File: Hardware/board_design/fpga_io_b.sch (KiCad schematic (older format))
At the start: 9 parts, among them P1 CONN_01X06, U1 XC7AxxT-xCSG325, U2 S25Q

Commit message: rescured and remaped symbols
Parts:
- C51: symbol C -> Device:C
- D2, D3, D4: symbol LED -> Device:LED
- P1: symbol CONN_01X06 -> PicoEVB-rescue:CONN_01X06-PicoEVB-rescue
- RN2, RN3: symbol R_Pack04 -> Device:R_Pack04
- U1: symbol xc7a50tcsg325 -> PicoEVB-rescue:xc7a50tcsg325-xc7a50t-bga325
- U2: symbol W25Q -> PicoEVB-rescue:W25Q-W25Q
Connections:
- wire segments 60 -> 74
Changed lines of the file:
@@
-EESchema Schematic File Version 2
-LIBS:power
-LIBS:device
-LIBS:transistors
-LIBS:conn
-LIBS:linear
-LIBS:regul
-LIBS:74xx
-LIBS:cmos4000
-LIBS:adc-dac
-LIBS:memory
-LIBS:xilinx
-LIBS:microcontrollers
-LIBS:dsp
-LIBS:microchip
-LIBS:analog_switches
-LIBS:motorola
-LIBS:texas
-LIBS:intel
-LIBS:audio
-LIBS:interface
-LIBS:digital-audio
-LIBS:philips
-LIBS:display
-LIBS:cypress
-LIBS:siliconi
-LIBS:opto
-LIBS:atmel
-LIBS:contrib
-LIBS:valves
-LIBS:Zilog
-LIBS:zetex
-LIBS:Xicor
-LIBS:Worldsemi
-LIBS:wiznet
-LIBS:video
-LIBS:ttl_ieee
-LIBS:transf
-LIBS:switches
-LIBS:supertex
-LIBS:stm32
-LIBS:stm8
-LIBS:silabs
-LIBS:sensors
-LIBS:rfcom
-LIBS:relays
-LIBS:references
-LIBS:pspice
-LIBS:Power_Management
-LIBS:powerint
-LIBS:Oscillators
-LIBS:onsemi
-LIBS:nxp_armmcu
-LIBS:nordicsemi
-LIBS:msp430
-LIBS:motors
-LIBS:motor_drivers
-LIBS:microchip_pic32mcu
-LIBS:microchip_pic18mcu
-LIBS:microchip_pic16mcu
-LIBS:microchip_pic12mcu
-LIBS:microchip_pic10mcu
-LIBS:microchip_dspic33dsc
-LIBS:mechanical
-LIBS:maxim
-LIBS:logo
-LIBS:Lattice
-LIBS:ir
-LIBS:hc11
-LIBS:graphic
-LIBS:gennum
-LIBS:ftdi
-LIBS:ESD_Protection
-LIBS:elec-unifil
-LIBS:diode
-LIBS:dc-dc
-LIBS:cmos_ieee
-LIBS:brooktre
-LIBS:bosch
-LIBS:bbd
-LIBS:battery_management
-LIBS:analog_devices
-LIBS:Altera
-LIBS:allegro
-LIBS:actel
-LIBS:ac-dc
-LIBS:74xgxx
-LIBS:xc7a50t-bga325
-LIBS:MAX1589A
-LIBS:MIC47050
-LIBS:TS3L110
-LIBS:W25Q
-LIBS:93LC46B-SOT23
-LIBS:m2-board
-LIBS:ft2232-fixed
-LIBS:tps82084
-LIBS:PicoEVB-cache
-EELAYER 25 0
+EESchema Schematic File Version 4
+EELAYER 30 0
 EELAYER END
-$Descr A 11000 8500
+$Descr A3 16535 11693
 encoding utf-8
 Sheet 4 7
@@
 $EndDescr
 $Comp
-L xc7a50tcsg325 U1
+L PicoEVB-rescue:xc7a50tcsg325-xc7a50t-bga325 U1
 U 4 1 586A5920
 P 5300 2900
@@
 $EndComp
 $Comp
-L xc7a50tcsg325 U1
+L PicoEVB-rescue:xc7a50tcsg325-xc7a50t-bga325 U1
 U 3 1 586A5977
 P 2550 1300
@@
 $EndComp
 $Comp
-L xc7a50tcsg325 U1
+L PicoEVB-rescue:xc7a50tcsg325-xc7a50t-bga325 U1
 U 2 1 594F31E6
 P 8600 1300
@@
 VCC_BANK14_B
 $Comp
-L GND #PWR023
+L power:GND #PWR023
 U 1 1 594F321A
 P 5650 1700
@@
 $EndComp
 $Comp
-L C C51
+L Device:C C51
 U 1 1 586D021A
 P 5950 1550
@@
 NoConn ~ 5300 7800
 $Comp
-L W25Q U2
+L PicoEVB-rescue:W25Q-W25Q U2
 U 1 1 587CA7B7
 P 6750 1400
@@
 NoConn ~ 8600 4100
 $Comp
-L LED D4
+L Device:LED D4
 U 1 1 587E337E
 P 8150 6000
@@
 $EndComp
 $Comp
-L LED D3
+L Device:LED D3
 U 1 1 594F3235
 P 8150 5700
@@
 $EndComp
 $Comp
-L LED D2
+L Device:LED D2
 U 1 1 587E3396
 P 8150 5300
@@
 NoConn ~ 8600 4800
 $Comp
-L CONN_01X06 P1
+L PicoEVB-rescue:CONN_01X06-PicoEVB-rescue P1
 U 1 1 59AB5657
 P 1350 4200
+AR Path="/59AB5657" Ref="P1"  Part="1"
+AR Path="/594F323A/59AB5657" Ref="P1"  Part="1"
 F 0 "P1" H 1350 4550 50  0000 C CNN
 F 1 "CONN_01X06" V 1450 4200 50  0000 C CNN
@@
 $EndComp
 $Comp
-L GND #PWR024
+L power:GND #PWR024
 U 1 1 59AB565E
 P 1400 4000
@@
 M2_LED_2
 Wire Wire Line
-	7250 6300 8600 6300
+	7250 6300 7400 6300
 Wire Wire Line
 	2400 6300 2550 6300
 Wire Wire Line
-	5800 1400 6450 1400
+	5800 1400 5950 1400
 Connection ~ 5950 1400
 Wire Wire Line
-	5650 1700 6450 1700
+	5650 1700 5950 1700
 Connection ~ 5950 1700
 Wire Wire Line
@@
 	6300 2300 6300 1600
 Wire Wire Line
-	6450 1500 6150 1500
+	6450 1500 6350 1500
 Wire Wire Line
 	6150 1500 6150 2400
@@
 	8600 1500 7250 1500
 Wire Wire Line
-	8600 1600 7250 1600
-Wire Wire Line
-	8600 1700 7250 1700
+	8600 1600 8000 1600
+Wire Wire Line
+	8600 1700 8100 1700
 Wire Wire Line
 	8350 1800 8600 1800
@@
 	5450 6100 5300 6100
 $Comp
-L R_Pack04 RN2
+L Device:R_Pack04 RN2
 U 1 1 59EAB957
 P 7600 5900
@@
 	7900 5300 8000 5300
 Wire Wire Line
-	7400 5700 7400 6300
+	7400 5700 7400 5800
 Connection ~ 7400 6300
 Connection ~ 7400 5800
@@
 	7800 6000 7800 6200
 $Comp
-L R_Pack04 RN3
+L Device:R_Pack04 RN3
 U 1 1 59EAF829
 P 7650 1100
@@
 	6200 850  7450 850
 Wire Wire Line
-	7450 850  7450 1200
+	7450 850  7450 900
 Connection ~ 6200 1400
 Connection ~ 7450 900
@@
 Connection ~ 8100 1700
 NoConn ~ 7850 900
+Wire Wire Line
+	5950 1400 6200 1400
+Wire Wire Line
+	5950 1700 6400 1700
+Wire Wire Line
+	6400 1700 6450 1700
+Wire Wire Line
+	7400 6300 8600 6300
+Wire Wire Line
+	7400 5800 7400 5900
+Wire Wire Line
+	7400 5900 7400 6000
+Wire Wire Line
+	7400 6000 7400 6300
+Wire Wire Line
+	6200 1400 6450 1400
+Wire Wire Line
+	7450 900  7450 1000
+Wire Wire Line
+	7450 1000 7450 1100
+Wire Wire Line
+	7450 1100 7450 1200
+Wire Wire Line
+	6350 1500 6150 1500
+Wire Wire Line
+	8000 1600 7250 1600
+Wire Wire Line
+	8100 1700 7250 1700
 $EndSCHEMATC

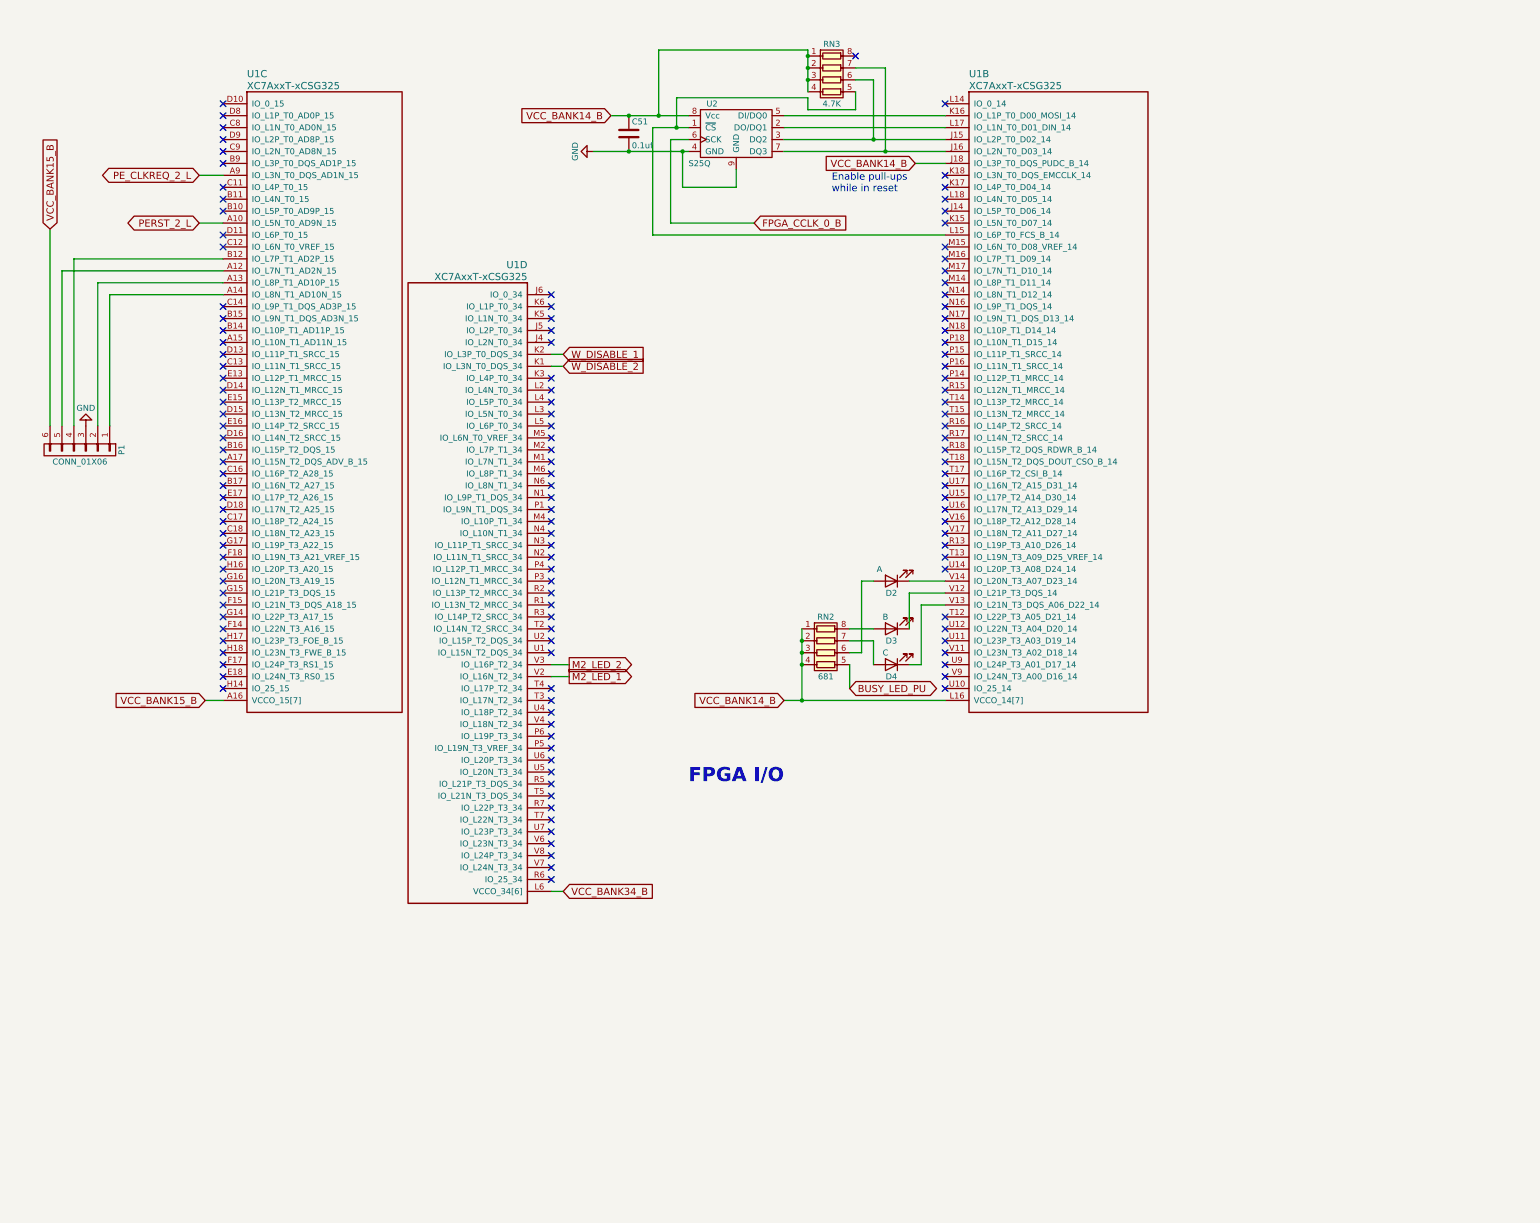
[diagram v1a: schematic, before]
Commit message: Added LPSDRAM
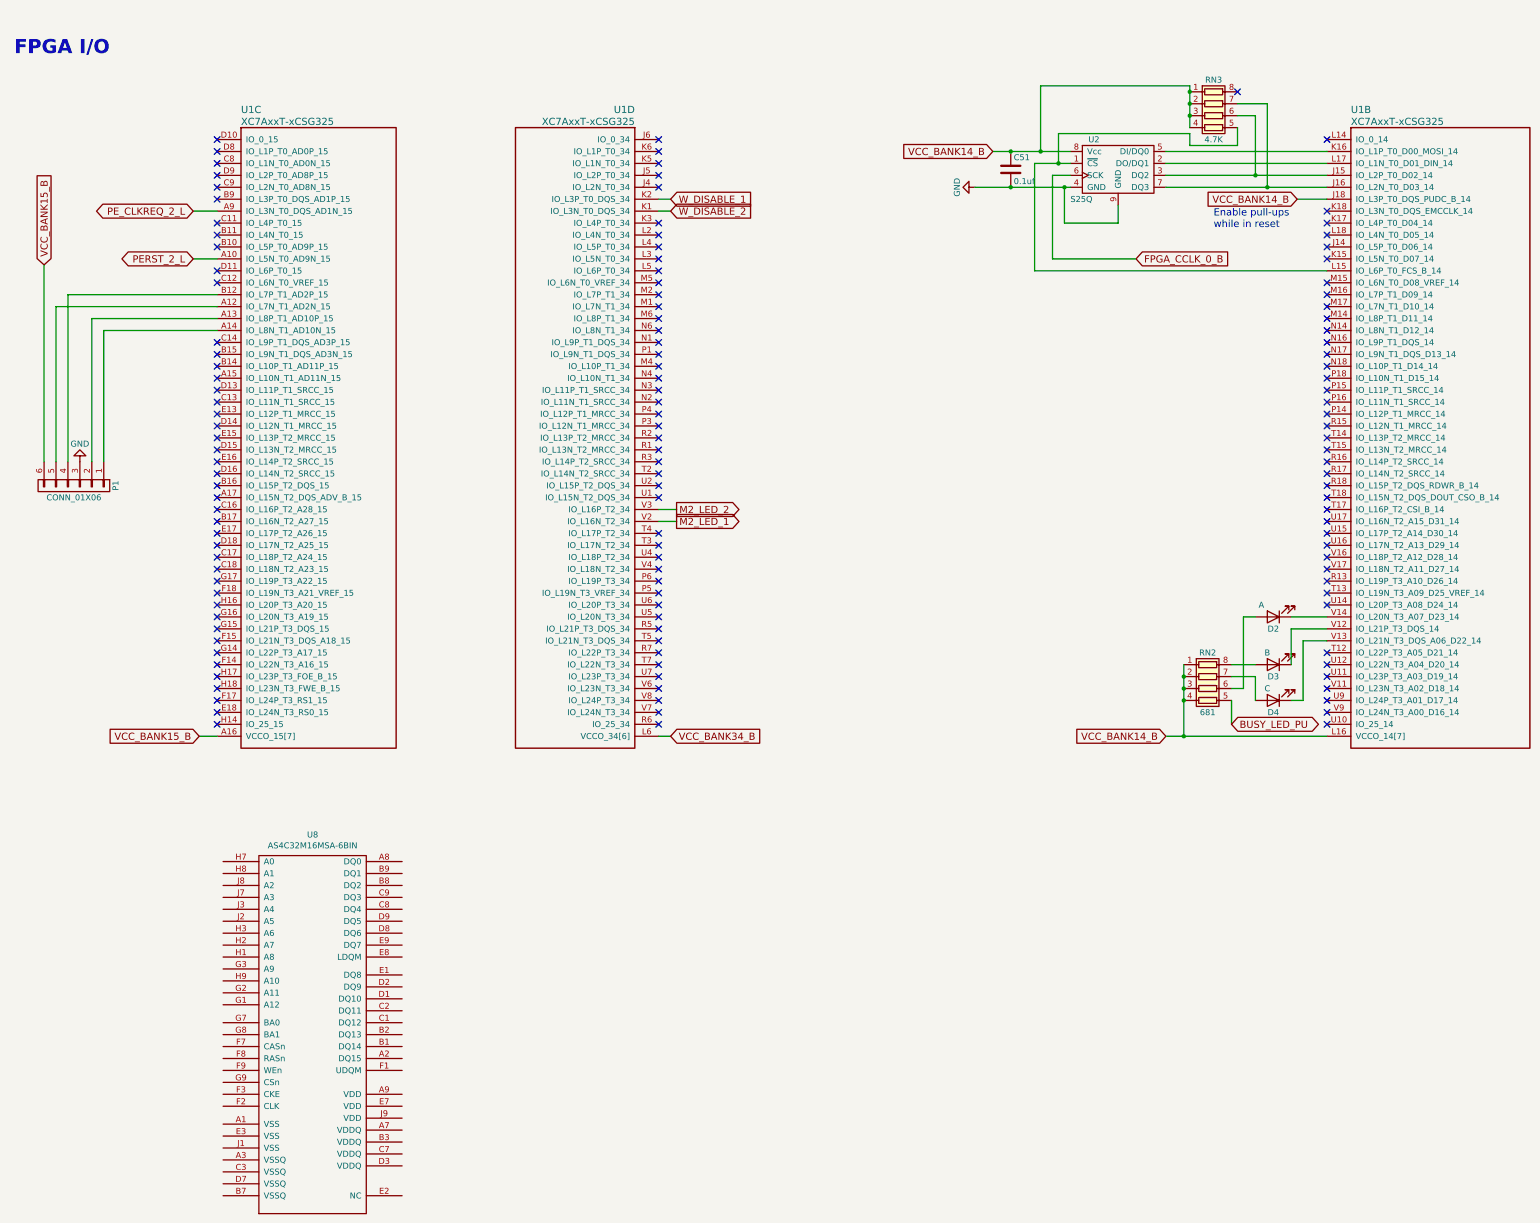
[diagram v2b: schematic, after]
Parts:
- added U8: AS4C32M16MSA-6BIN, AS4C32M16MSA-6BIN:AS4C32M16MSA-6BIN, symbol AS4C32M16MSA-6BIN:AS4C32M16MSA-6BIN
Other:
- moved on the sheet: C51, D2, D3, D4, P1, RN2, RN3, U1B, U1C, U1D, U2
